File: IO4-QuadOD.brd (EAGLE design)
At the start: 100 x 100 mm, 21 parts, among them CON10 5MM, CON3 5MM, CON9 CONNECTOR-I2CLEFT

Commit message: added values for connectors
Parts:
- CON1: value (none) -> 2.1mm
- MCU: value (none) -> Mini
- X1, X2, X3, X4: value (none) -> 0.156
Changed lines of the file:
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@@
 <setting verticaltext="up"/>
 </settings>
-<grid distance="50" unitdist="mil" unit="mil" style="dots" multiple="2" display="yes" altdistance="5" altunitdist="mil" altunit="mil"/>
+<grid distance="50" unitdist="mil" unit="mil" style="dots" multiple="2" display="yes" altdistance="25" altunitdist="mil" altunit="mil"/>
 <layers>
 <layer number="1" name="Top" color="4" fill="1" visible="yes" active="yes"/>
@@
 <attribute name="VALUE" x="59.69" y="-1.27" size="0.4064" layer="27" font="vector" rot="R180"/>
 </element>
-<element name="X1" library="SPCoast" package="KK-156-5" value="" x="13.97" y="57.785" smashed="yes" rot="R270">
+<element name="X1" library="SPCoast" package="KK-156-5" value="0.156" x="13.97" y="57.785" smashed="yes" rot="R270">
 <attribute name="OC_FARNELL" value="unknown" x="13.97" y="57.785" size="0.254" layer="27" rot="R270" display="off"/>
 <attribute name="OC_NEWARK" value="unknown" x="13.97" y="57.785" size="0.254" layer="27" rot="R270" display="off"/>
@@
 <attribute name="VALUE" x="9.525" y="46.095" size="1.27" layer="27"/>
 </element>
-<element name="X2" library="SPCoast" package="KK-156-5" value="" x="39.37" y="57.785" smashed="yes" rot="R270">
+<element name="X2" library="SPCoast" package="KK-156-5" value="0.156" x="39.37" y="57.785" smashed="yes" rot="R270">
 <attribute name="OC_FARNELL" value="unknown" x="39.37" y="57.785" size="0.254" layer="27" rot="R270" display="off"/>
 <attribute name="OC_NEWARK" value="unknown" x="39.37" y="57.785" size="0.254" layer="27" rot="R270" display="off"/>
@@
 <attribute name="VALUE" x="34.925" y="46.095" size="1.27" layer="27"/>
 </element>
-<element name="X3" library="SPCoast" package="KK-156-5" value="" x="64.77" y="57.785" smashed="yes" rot="R270">
+<element name="X3" library="SPCoast" package="KK-156-5" value="0.156" x="64.77" y="57.785" smashed="yes" rot="R270">
 <attribute name="OC_FARNELL" value="unknown" x="64.77" y="57.785" size="0.254" layer="27" rot="R270" display="off"/>
 <attribute name="OC_NEWARK" value="unknown" x="64.77" y="57.785" size="0.254" layer="27" rot="R270" display="off"/>
@@
 <attribute name="VALUE" x="60.325" y="46.095" size="1.27" layer="27"/>
 </element>
-<element name="X4" library="SPCoast" package="KK-156-5" value="" x="90.17" y="57.785" smashed="yes" rot="R270">
+<element name="X4" library="SPCoast" package="KK-156-5" value="0.156" x="90.17" y="57.785" smashed="yes" rot="R270">
 <attribute name="OC_FARNELL" value="unknown" x="90.17" y="57.785" size="0.254" layer="27" rot="R270" display="off"/>
 <attribute name="OC_NEWARK" value="unknown" x="90.17" y="57.785" size="0.254" layer="27" rot="R270" display="off"/>
@@
 <attribute name="VALUE" x="85.725" y="46.095" size="1.27" layer="27"/>
 </element>
-<element name="MCU" library="SPCoast" package="WEMOS-D1" value="" x="29.21" y="13.97" smashed="yes">
+<element name="MCU" library="SPCoast" package="WEMOS-D1" value="Mini" x="29.21" y="13.97" smashed="yes">
 <attribute name="NAME" x="30.48" y="30.48" size="1.27" layer="25" font="vector" rot="SR180"/>
 <attribute name="VALUE" x="40.64" y="-1.27" size="1.27" layer="27" rot="SR180"/>
@@
 </element>
 <element name="CON10" library="SPCoast" package="SCREWTERMINAL-5MM-3" value="5MM" x="74.295" y="23.495" rot="R180"/>
-<element name="CON1" library="SPCoast" package="DCJ0202" value="" x="83.82" y="17.78"/>
+<element name="CON1" library="SPCoast" package="DCJ0202" value="2.1mm" x="83.82" y="17.78"/>
 <element name="MT1" library="SPCoast" package="MOUNTINGHOLE" value="MOUNTINGHOLE" x="5.08" y="5.08"/>
 <element name="MT2" library="SPCoast" package="MOUNTINGHOLE" value="MOUNTINGHOLE" x="95.25" y="5.08"/>

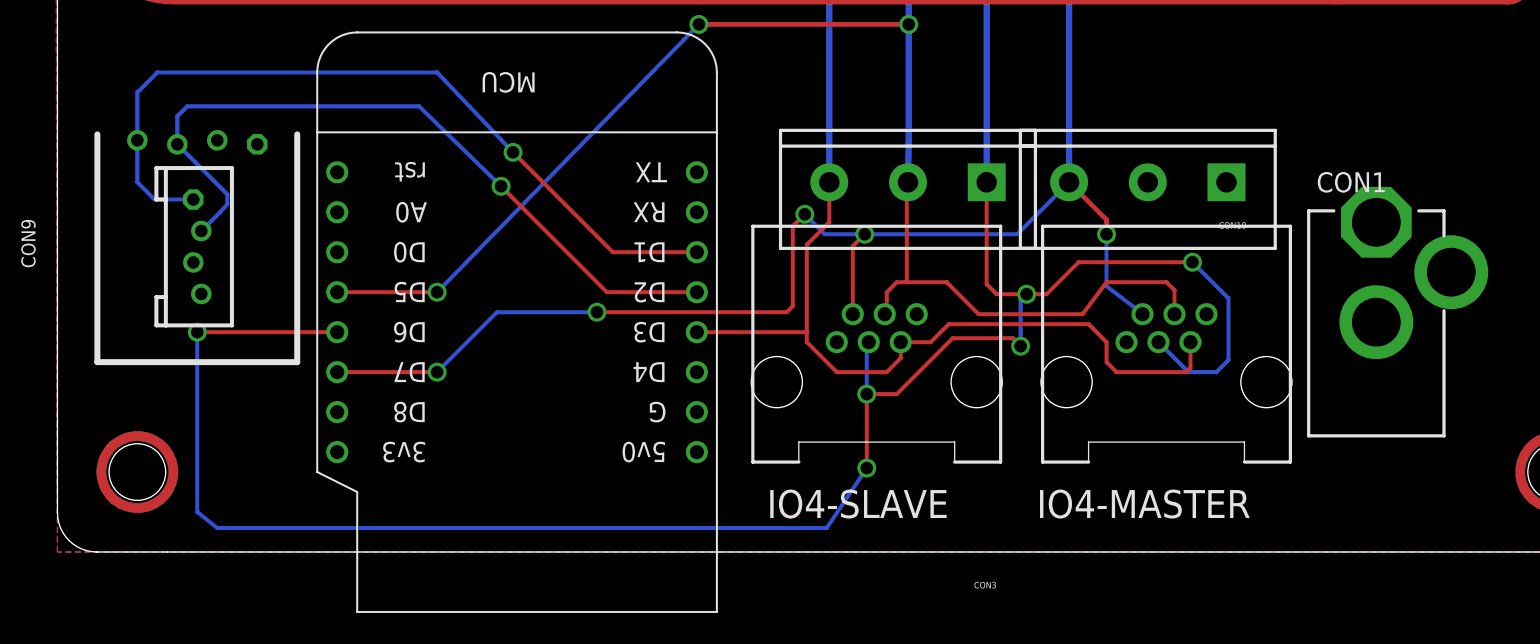
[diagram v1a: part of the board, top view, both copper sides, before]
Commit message: normalized values
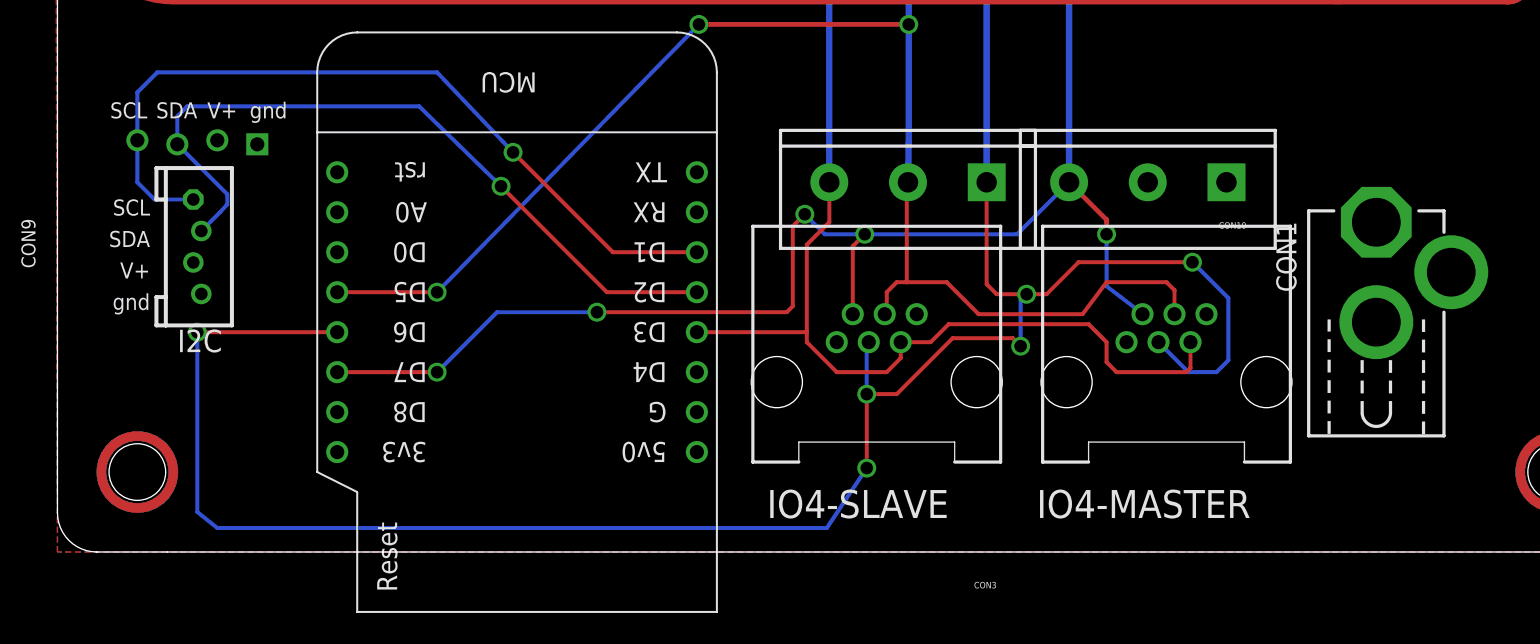
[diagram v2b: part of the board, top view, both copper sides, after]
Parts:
- BOARD1: value BOARD100X100-NOHOLES -> BOARD
- CON9: value CONNECTOR-I2CLEFT -> (none)
- DCCIN, TK1, TK2, TK3, TK4: value MSTBA2 -> 0.200
- IO4-MASTER, IO4-SLAVE: value RJ12-INV -> RJ12/6
- MCU: value Mini -> Mini-R2
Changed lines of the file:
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@@
 </autorouter>
 <elements>
-<element name="BOARD1" library="SPCoast" package="BOARD-SEEED10X10-NOHOLES" value="BOARD100X100-NOHOLES" x="0" y="0" smashed="yes"/>
-<element name="DCCIN" library="SPCoast" package="MSTBA2" value="MSTBA2" x="15.24" y="88.265" smashed="yes" rot="R180">
+<element name="BOARD1" library="SPCoast" package="BOARD-SEEED10X10-NOHOLES" value="BOARD" x="0" y="0" smashed="yes"/>
+<element name="DCCIN" library="SPCoast" package="MSTBA2" value="0.200" x="15.24" y="88.265" smashed="yes" rot="R180">
 <attribute name="MF" value="FARNELL" x="15.24" y="88.265" size="1.778" layer="27" rot="R180" display="off"/>
 <attribute name="OC_NEWARK" value="71C4161" x="15.24" y="88.265" size="1.778" layer="27" rot="R180" display="off"/>
@@
 <attribute name="VALUE" x="20.32" y="88.265" size="1.778" layer="27" font="vector" ratio="10" rot="R180"/>
 </element>
-<element name="TK1" library="SPCoast" package="MSTBA2" value="MSTBA2" x="31.75" y="88.265" smashed="yes" rot="R180">
+<element name="TK1" library="SPCoast" package="MSTBA2" value="0.200" x="31.75" y="88.265" smashed="yes" rot="R180">
 <attribute name="MF" value="FARNELL" x="31.75" y="88.265" size="1.778" layer="27" rot="R180" display="off"/>
 <attribute name="OC_NEWARK" value="71C4161" x="31.75" y="88.265" size="1.778" layer="27" rot="R180" display="off"/>
@@
 <attribute name="VALUE" x="36.83" y="88.265" size="1.778" layer="27" font="vector" ratio="10" rot="R180"/>
 </element>
-<element name="TK2" library="SPCoast" package="MSTBA2" value="MSTBA2" x="49.53" y="88.265" smashed="yes" rot="R180">
+<element name="TK2" library="SPCoast" package="MSTBA2" value="0.200" x="49.53" y="88.265" smashed="yes" rot="R180">
 <attribute name="MF" value="FARNELL" x="49.53" y="88.265" size="1.778" layer="27" rot="R180" display="off"/>
 <attribute name="OC_NEWARK" value="71C4161" x="49.53" y="88.265" size="1.778" layer="27" rot="R180" display="off"/>
@@
 <attribute name="VALUE" x="54.61" y="88.265" size="1.778" layer="27" font="vector" ratio="10" rot="R180"/>
 </element>
-<element name="TK3" library="SPCoast" package="MSTBA2" value="MSTBA2" x="67.31" y="88.265" smashed="yes" rot="R180">
+<element name="TK3" library="SPCoast" package="MSTBA2" value="0.200" x="67.31" y="88.265" smashed="yes" rot="R180">
 <attribute name="MF" value="FARNELL" x="67.31" y="88.265" size="1.778" layer="27" rot="R180" display="off"/>
 <attribute name="OC_NEWARK" value="71C4161" x="67.31" y="88.265" size="1.778" layer="27" rot="R180" display="off"/>
@@
 <attribute name="VALUE" x="72.39" y="88.265" size="1.778" layer="27" font="vector" ratio="10" rot="R180"/>
 </element>
-<element name="TK4" library="SPCoast" package="MSTBA2" value="MSTBA2" x="85.09" y="88.265" smashed="yes" rot="R180">
+<element name="TK4" library="SPCoast" package="MSTBA2" value="0.200" x="85.09" y="88.265" smashed="yes" rot="R180">
 <attribute name="MF" value="FARNELL" x="85.09" y="88.265" size="1.778" layer="27" rot="R180" display="off"/>
 <attribute name="OC_NEWARK" value="71C4161" x="85.09" y="88.265" size="1.778" layer="27" rot="R180" display="off"/>
@@
 <attribute name="VALUE" x="90.17" y="88.265" size="1.778" layer="27" font="vector" ratio="10" rot="R180"/>
 </element>
-<element name="IO4-SLAVE" library="SPCoast" package="RJ25-INVERTED" value="RJ12-INV" x="52.07" y="10.795" smashed="yes">
+<element name="IO4-SLAVE" library="SPCoast" package="RJ25-INVERTED" value="RJ12/6" x="52.07" y="10.795" smashed="yes">
 <attribute name="NAME" x="45.085" y="2.159" size="1.778" layer="25" font="vector"/>
 <attribute name="VALUE" x="45.847" y="-2.54" size="1.778" layer="27" font="vector"/>
 </element>
-<element name="IO4-MASTER" library="SPCoast" package="RJ25-INVERTED" value="RJ12-INV" x="70.485" y="10.795" smashed="yes">
+<element name="IO4-MASTER" library="SPCoast" package="RJ25-INVERTED" value="RJ12/6" x="70.485" y="10.795" smashed="yes">
 <attribute name="NAME" x="62.23" y="2.159" size="1.778" layer="25" font="vector"/>
 <attribute name="VALUE" x="63.627" y="-2.54" size="1.778" layer="27" font="vector"/>
@@
 <attribute name="VALUE" x="85.725" y="46.095" size="1.27" layer="27"/>
 </element>
-<element name="MCU" library="SPCoast" package="WEMOS-D1" value="Mini" x="29.21" y="13.97" smashed="yes">
+<element name="MCU" library="SPCoast" package="WEMOS-D1" value="Mini-R2" x="29.21" y="13.97" smashed="yes">
 <attribute name="NAME" x="30.48" y="30.48" size="1.27" layer="25" font="vector" rot="SR180"/>
 <attribute name="VALUE" x="40.64" y="-1.27" size="1.27" layer="27" rot="SR180"/>
 </element>
-<element name="CON9" library="SPCoast" package="I2C-L" value="CONNECTOR-I2CLEFT" x="8.89" y="26.035" smashed="yes">
+<element name="CON9" library="SPCoast" package="I2C-L" value="" x="8.89" y="26.035" smashed="yes">
 <attribute name="NAME" x="-1.397" y="18.034" size="0.889" layer="25" font="vector" ratio="11" rot="R90"/>
 <attribute name="VALUE" x="-2.032" y="15.494" size="0.635" layer="27" font="vector" ratio="10" rot="R90"/>
